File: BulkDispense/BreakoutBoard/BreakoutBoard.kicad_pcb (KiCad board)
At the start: 2 copper layers, 170 x 100.5 mm, 33 parts, among them J1 Bubble Sensor Power, J10 Reagent Media Valve Signal, J11 Proportional Control Valve, J12 Reagent Media Valve GND, J13 Pressure Sensor, J14 Waste 2/2 Media Valve GND, J15 Waste 2/2 Media Valve Power, J16 Waste 3/2 Media Valve, J17 Waste Bottle Sensor 1, J18 Waste Line Sensor 2, J19 Waste Line Sensor 1, J2 Bubble Sensor Signal, J20 Waste Bottle Sensor 2, J21 Waste Vacuum Sensor 1, J22 Waste Vacuum Sensor 2, J23 MAXI Power, J24 Waste 2/2 Media Valve Power, J25 Waste 2/2 Media Valve GND, J26 Waste Line Sensor 1, J27 Waste Line Sensor 2, J28 Waste Bottle Sensor 1, J29 Waste Bottle Sensor 2, J3 Bubble Sensor GND, J30 Waste 3/2 Media Valve, J31 Waste Vacuum Sensor 1, J32 Waste Vacuum Sensor 2, J33 37212-62M3-003PL, J4 Overflow Sensor Power, J5 Overflow Sensor GND, J6 Overflow Sensor Signal, J7 Input Power, J8 Reagent Valve Power, J9 Reagent Valve GND

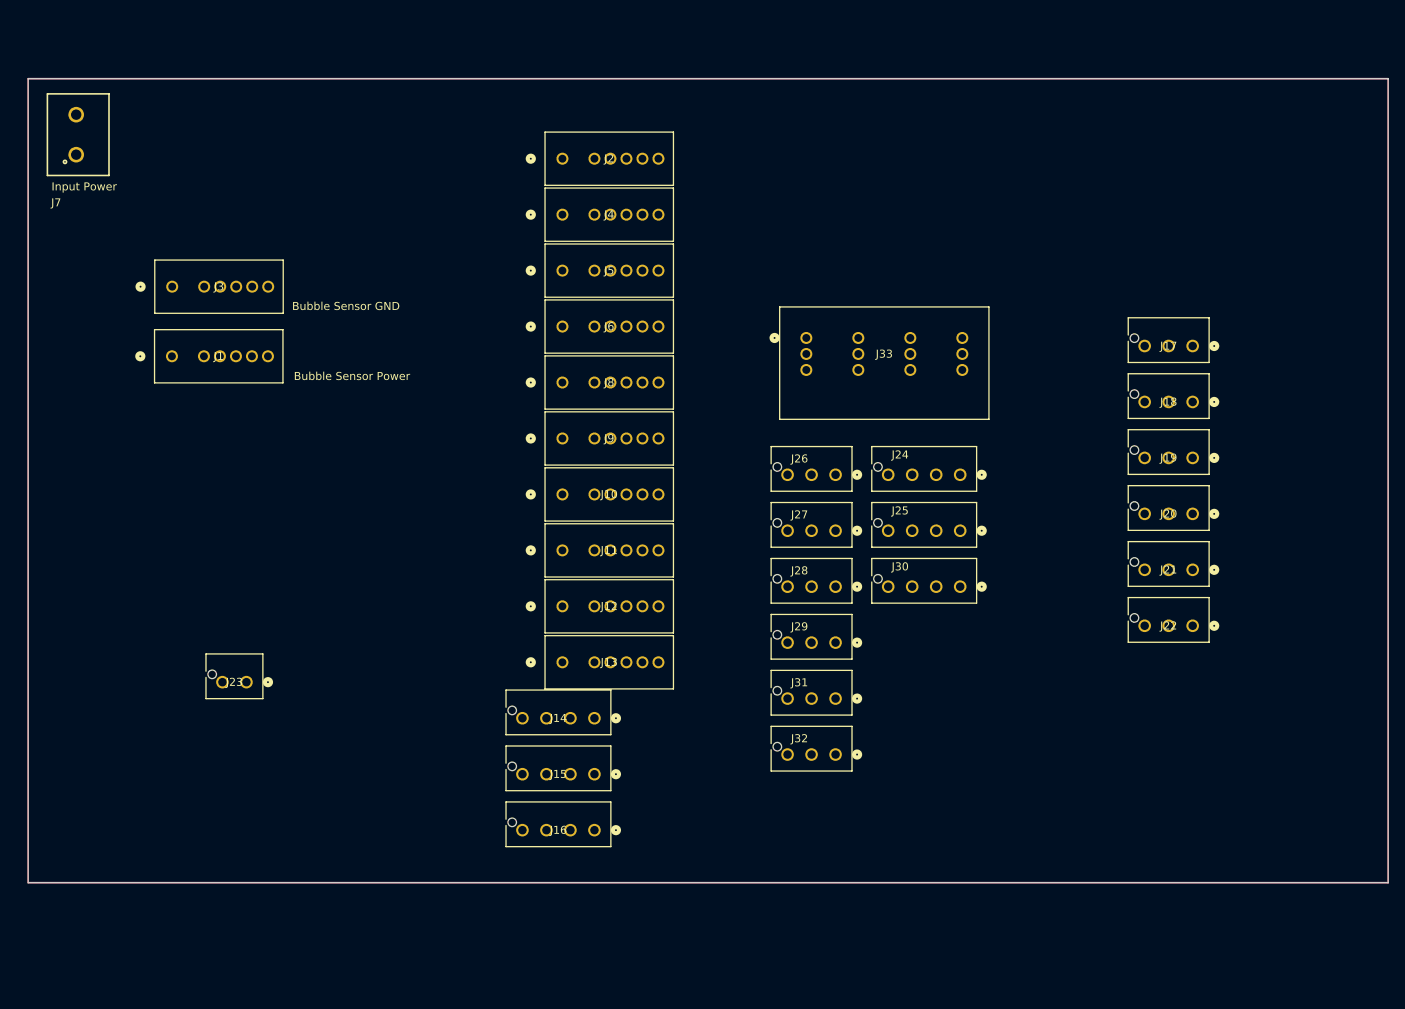
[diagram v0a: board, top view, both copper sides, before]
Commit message: Update 3POS Connectors with Mini-Clamp
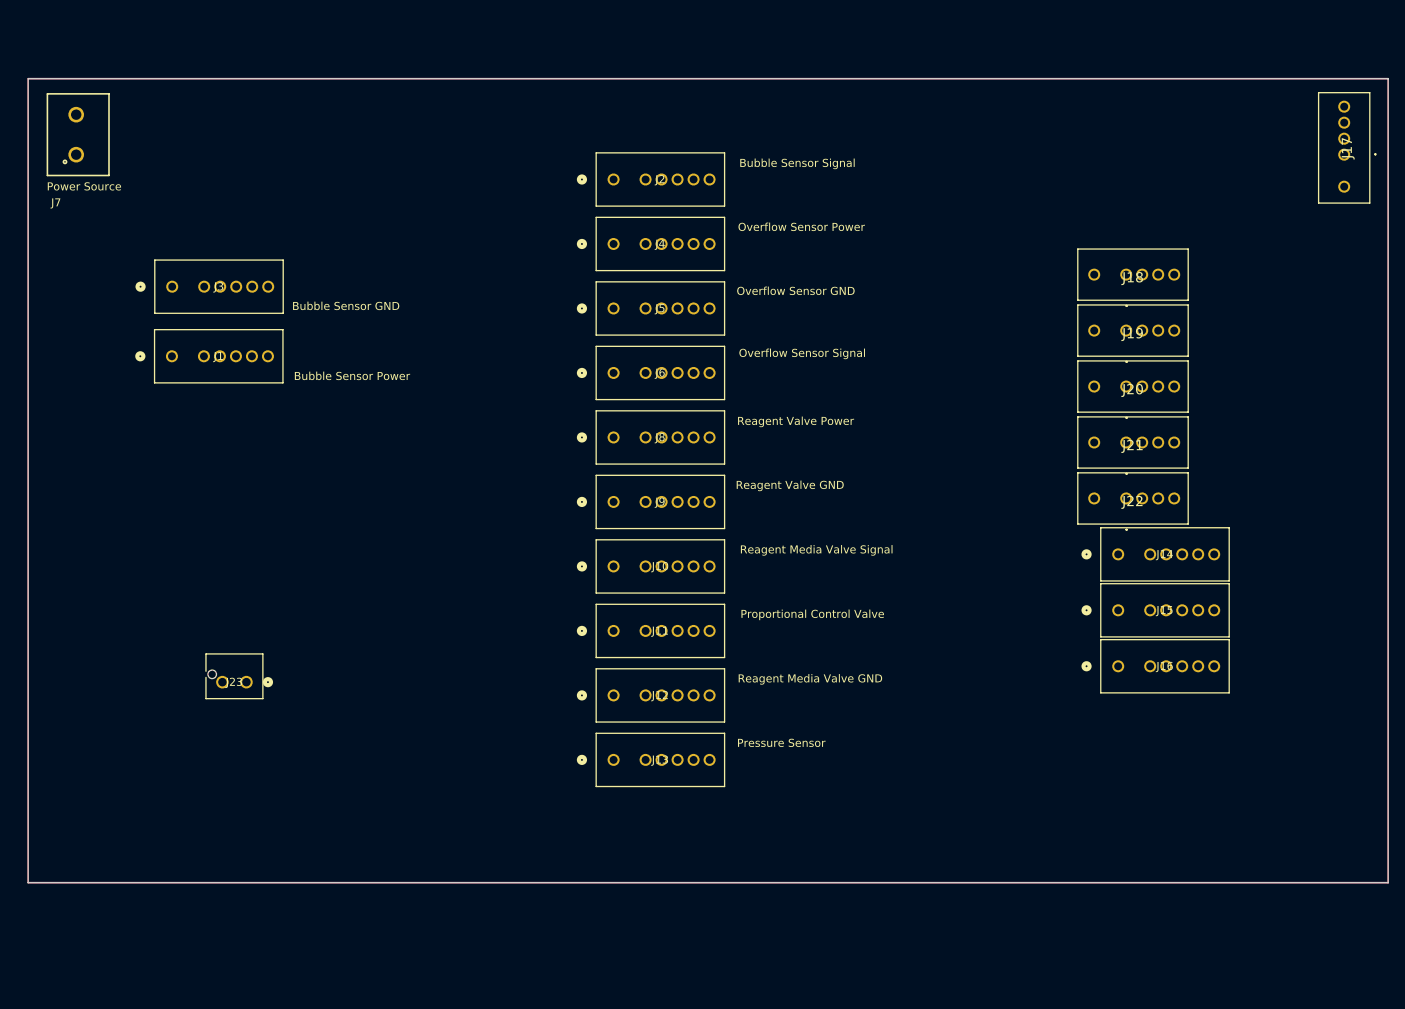
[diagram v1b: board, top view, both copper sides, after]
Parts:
- removed J24: Waste 2/2 Media Valve Power, PartsLibrary:CONN04_2165712004_MOL
- removed J25: Waste 2/2 Media Valve GND, PartsLibrary:CONN04_2165712004_MOL
- removed J26: Waste Line Sensor 1, PartsLibrary:CONN03_2165711003_MOL
- removed J27: Waste Line Sensor 2, PartsLibrary:CONN03_2165711003_MOL
- removed J28: Waste Bottle Sensor 1, PartsLibrary:CONN03_2165711003_MOL
- removed J29: Waste Bottle Sensor 2, PartsLibrary:CONN03_2165711003_MOL
- removed J30: Waste 3/2 Media Valve, PartsLibrary:CONN04_2165712004_MOL
- removed J31: Waste Vacuum Sensor 1, PartsLibrary:CONN03_2165711003_MOL
- removed J32: Waste Vacuum Sensor 2, PartsLibrary:CONN03_2165711003_MOL
- removed J33: 37212-62M3-003PL, PartsLibrary:CONN_37212-62M3-003PL_3MM
- J14, J15, J16: footprint PartsLibrary:CONN04_2165712004_MOL -> PartsLibrary:CONN_37204-62A3-004PL_3MM
- J17, J18, J19, J20, J21, J22: footprint PartsLibrary:CONN03_2165711003_MOL -> PartsLibrary:3720362A3003PL
- J7: value Input Power -> Power Source
- moved J14 72.4 mm to (191.7, 96.5)
- moved J15 72.4 mm to (191.7, 103.5)
- moved J16 72.4 mm to (191.7, 110.4)
- moved J17 30.5 mm to (216.0, 46.5), turned to 90 degrees
- moved J18 18.0 mm to (188.8, 61.5)
- moved J19 18.0 mm to (188.8, 68.5)
- moved J20 18.0 mm to (188.8, 75.5)
- moved J21 18.0 mm to (188.8, 82.5)
- moved J22 18.0 mm to (188.8, 89.5)
- moved J13 13.8 mm to (128.7, 122.2)
- moved J12 12.8 mm to (128.7, 114.1)
- moved J11 11.9 mm to (128.7, 106.0)
- moved J10 11.0 mm to (128.7, 98.0)
- moved J9 10.2 mm to (128.7, 89.9)
- moved J8 9.38 mm to (128.7, 81.8)
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
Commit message: First Draft of BreakoutBoard
- Included MAXI Expansion Board Starter
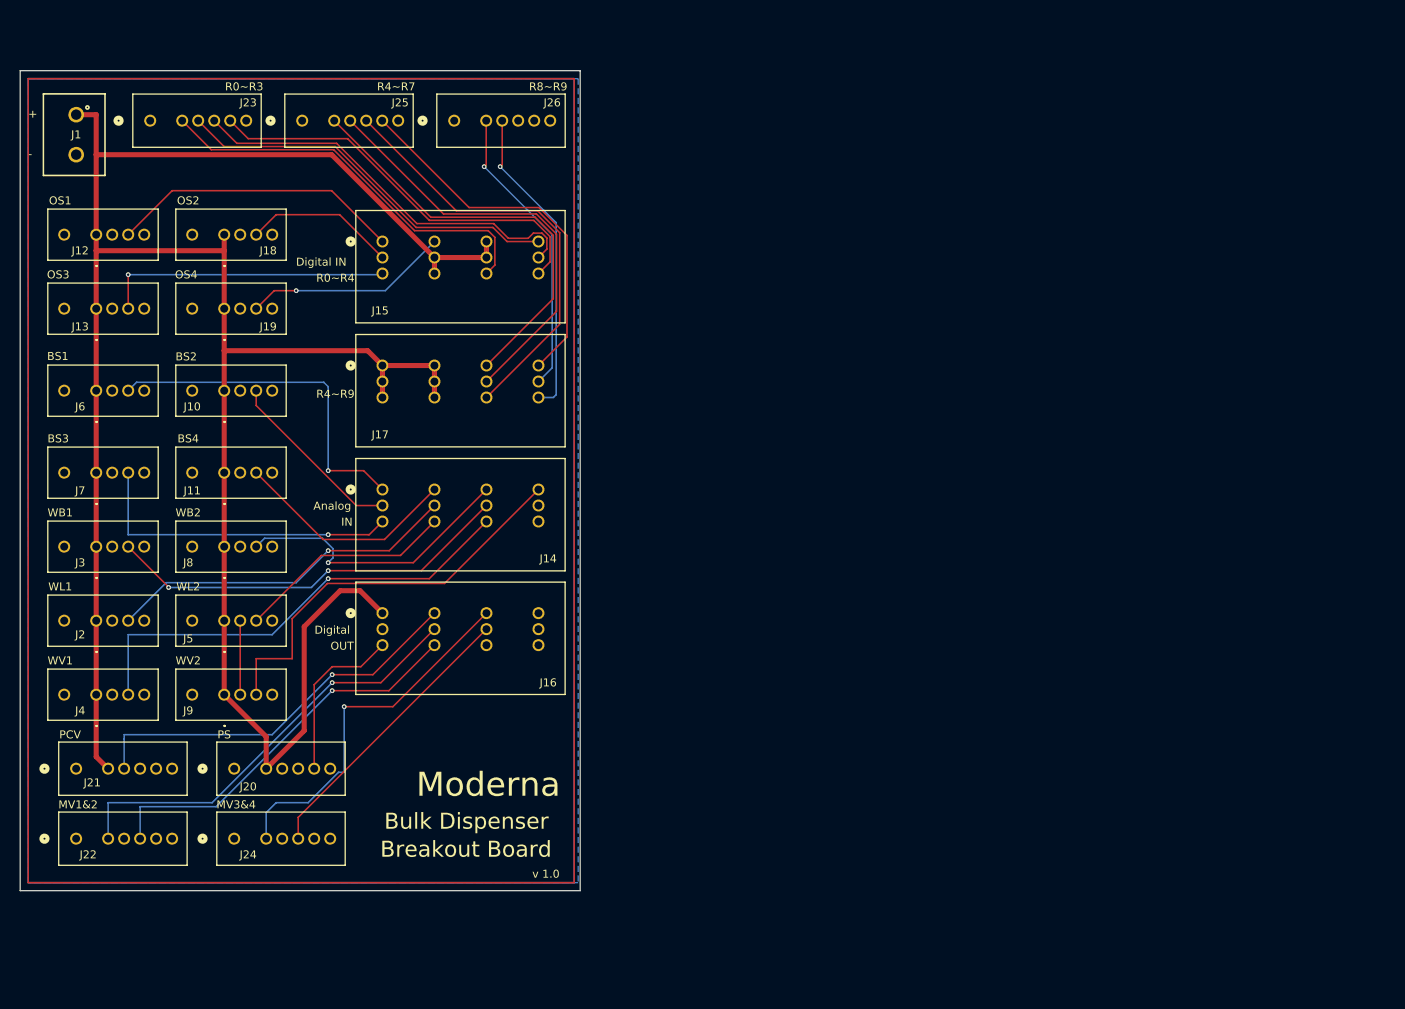
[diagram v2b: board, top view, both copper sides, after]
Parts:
- removed the J1 at (73.5, 71.7)
- added J24: MV3&4, PartsLibrary:CONN_37204-62A3-004PL_3MM, F.Cu at (81.2, 132.0)
- added J25: R4~R7, PartsLibrary:CONN_37204-62A3-004PL_3MM, F.Cu at (89.8, 42.2)
- added J26: R8~R9, PartsLibrary:CONN_37204-62A3-004PL_3MM, F.Cu at (108.8, 42.2)
- added J7: BS3, PartsLibrary:3720362A3003PL, F.Cu at (60.0, 86.2)
- J10: value Reagent Media Valve Signal -> BS2; footprint PartsLibrary:CONN_37204-62A3-004PL_3MM -> PartsLibrary:3720362A3003PL
- J11: value Proportional Control Valve -> BS4; footprint PartsLibrary:CONN_37204-62A3-004PL_3MM -> PartsLibrary:3720362A3003PL
- J12: value Reagent Media Valve GND -> OS1; footprint PartsLibrary:CONN_37204-62A3-004PL_3MM -> PartsLibrary:3720362A3003PL
- J13: value Pressure Sensor -> OS3; footprint PartsLibrary:CONN_37204-62A3-004PL_3MM -> PartsLibrary:3720362A3003PL
- J14: value Waste 2/2 Media Valve GND -> Analog Inputs; footprint PartsLibrary:CONN_37204-62A3-004PL_3MM -> PartsLibrary:CONN_37212-62M3-003PL_3MM
- J15: value Waste 2/2 Media Valve Power -> Digital IN + R0~R4; footprint PartsLibrary:CONN_37204-62A3-004PL_3MM -> PartsLibrary:CONN_37212-62M3-003PL_3MM
- J16: value Waste 3/2 Media Valve -> Digital Outputs; footprint PartsLibrary:CONN_37204-62A3-004PL_3MM -> PartsLibrary:CONN_37212-62M3-003PL_3MM
- J17: value Waste Bottle Sensor 1 -> R4~R9; footprint PartsLibrary:3720362A3003PL -> PartsLibrary:CONN_37212-62M3-003PL_3MM
- J18: value Waste Line Sensor 2 -> OS2
- J19: value Waste Line Sensor 1 -> OS4
- J2: value Bubble Sensor Signal -> WL1; footprint PartsLibrary:CONN_37204-62A3-004PL_3MM -> PartsLibrary:3720362A3003PL
- J20: value Waste Bottle Sensor 2 -> PS; footprint PartsLibrary:3720362A3003PL -> PartsLibrary:CONN_37204-62A3-004PL_3MM
- J21: value Waste Vacuum Sensor 1 -> PCV; footprint PartsLibrary:3720362A3003PL -> PartsLibrary:CONN_37204-62A3-004PL_3MM
- J22: value Waste Vacuum Sensor 2 -> MV1&2; footprint PartsLibrary:3720362A3003PL -> PartsLibrary:CONN_37204-62A3-004PL_3MM
- J23: value MAXI Power -> R0~R3; footprint PartsLibrary:CONN02_2165711002_MOL -> PartsLibrary:CONN_37204-62A3-004PL_3MM
- J3: value Bubble Sensor GND -> WB1; footprint PartsLibrary:CONN_37204-62A3-004PL_3MM -> PartsLibrary:3720362A3003PL
- J4: value Overflow Sensor Power -> WV1; footprint PartsLibrary:CONN_37204-62A3-004PL_3MM -> PartsLibrary:3720362A3003PL
- J5: value Overflow Sensor GND -> WL2; footprint PartsLibrary:CONN_37204-62A3-004PL_3MM -> PartsLibrary:3720362A3003PL
- J6: value Overflow Sensor Signal -> BS1; footprint PartsLibrary:CONN_37204-62A3-004PL_3MM -> PartsLibrary:3720362A3003PL
- J8: value Reagent Valve Power -> WB2; footprint PartsLibrary:CONN_37204-62A3-004PL_3MM -> PartsLibrary:3720362A3003PL
- J9: value Reagent Valve GND -> WV2; footprint PartsLibrary:CONN_37204-62A3-004PL_3MM -> PartsLibrary:3720362A3003PL
- moved J22 134.2 mm to (61.5, 132.0)
- moved J21 133.6 mm to (61.5, 123.2)
- moved J17 123.1 mm to (95.8, 72.9), turned to 0 degrees
- moved J20 117.6 mm to (81.2, 123.2)
- moved J18 112.9 mm to (76.0, 56.5)
- moved J19 112.8 mm to (76.0, 65.8)
- moved J15 106.5 mm to (95.8, 57.4)
- moved J14 96.3 mm to (95.8, 88.4)
- moved J16 96.2 mm to (95.8, 103.8)
- moved J12 89.6 mm to (60.0, 56.5)
- moved J13 88.9 mm to (60.0, 65.8)
- moved J4 88.8 mm to (60.0, 114.0)
- moved J2 88.1 mm to (60.0, 104.8)
- moved J23 70.6 mm to (70.8, 42.2)
- moved J6 68.7 mm to (60.0, 76.0)
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- renumbered J7 to J1
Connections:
- J10 pad 1: /DO3 -> +24V
- J10 pad 2: /DO2 -> GND
- J10 pad 3: /DO1 -> /AI1
- J11 pad 2: /AI13 -> GND
- J11 pad 3: /AO0 -> /AI3
- J12 pad 1: GND -> +24V
- J12 pad 3: GND -> /DI0
- J13 pad 3: GND -> /DI2
- J14 pad 1: GND -> /AI0
- J14 pad 2: GND -> /AI1
- J14 pad 3: GND -> /AI2
- J14 pad 4: GND -> /AI3
- J14 pad 5: (no net) -> /AI4
- J14 pad 6: (no net) -> /AI5
- J15 pad 1: +24V -> /DI0
- J15 pad 2: +24V -> /DI1
- J15 pad 3: +24V -> /DI2
- J15 pad 4: +24V -> /DI3
- J15 pad 5: (no net) -> +24V
- J15 pad 6: (no net) -> +24V
- J16 pad 2: +24V -> GND
- J16 pad 3: GND -> /AI12
- J16 pad 4: GND -> /AI13
- J16 pad 5: (no net) -> /DO0
- J16 pad 6: (no net) -> /DO1
- J17 pad 2: GND -> +24V
- J17 pad 3: /AI7 -> +24V
- J18 pad 3: /AI5 -> /DI1
- J19 pad 3: /AI4 -> /DI3
- J2 pad 1: /AI3 -> +24V
- J2 pad 2: /AI2 -> GND
- J2 pad 3: /AI1 -> /AI4
- J20 pad 3: /AI6 -> GND
- J21 pad 2: GND -> /AI13
- J21 pad 3: /AI8 -> /AO0
- J22 pad 1: +24V -> /DO0
- J22 pad 3: /AI9 -> /DO1
- J23 pad 1: +24V -> /R0_OUT
- J23 pad 2: GND -> /R1_OUT
- J3 pad 1: GND -> +24V
- J3 pad 3: GND -> /AI7
- J4 pad 2: +24V -> GND
- J4 pad 3: +24V -> /AI8
- J5 pad 1: GND -> +24V
- J5 pad 3: GND -> /AI5
- J6 pad 1: /DI3 -> +24V
- J6 pad 2: /DI2 -> GND
- J6 pad 3: /DI1 -> /AI0
- J8 pad 2: +24V -> GND
- J8 pad 3: +24V -> /AI6
- J9 pad 1: GND -> +24V
- J9 pad 3: GND -> /AI9
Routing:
- net +24V: track 0.00 -> 295.5 mm
- net /AI8: track 0.00 -> 58.3 mm, vias 0 -> 1
- net /R6_OUT: track 0.00 -> 54.4 mm
- net /DO0: track 0.00 -> 54.3 mm, vias 0 -> 1
- net /R5_OUT: track 0.00 -> 53.7 mm
- net /R4_OUT: track 0.00 -> 53.1 mm
- net /AI9: track 0.00 -> 51.5 mm
- net /R3_OUT: track 0.00 -> 51.2 mm
- net /AI7: track 0.00 -> 51.2 mm, vias 0 -> 2
- net /R2_OUT: track 0.00 -> 51.1 mm
- net /R0_OUT: track 0.00 -> 50.1 mm
- net /AI13: track 0.00 -> 49.3 mm, vias 0 -> 1
- net /DO1: track 0.00 -> 49.2 mm, vias 0 -> 1
- net /R1_OUT: track 0.00 -> 48.8 mm
- net /R7_OUT: track 0.00 -> 46.8 mm
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- added copper zone on B.Cu, net GND
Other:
- board size 170 x 100.5 mm -> 70 x 102.5 mm
- board text added: "+"
- board text added: "-"
- board text added: "Analog"
- board text added: "Breakout Board"
- board text added: "Bulk Dispenser"
- board text added: "Digital"
- board text added: "Digital IN"
- board text added: "IN"
- board text added: "Moderna"
- board text added: "OUT"
- board text added: "R0~R4"
- board text added: "R4~R9"
- board text added: "v 1.0"

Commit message: Add more documentation + holding mounts
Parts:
- added H1: MountingHole, MountingHole:MountingHole_2.2mm_M2, F.Cu at (120.5, 37.0)
- added H2: MountingHole, MountingHole:MountingHole_2.2mm_M2, F.Cu at (51.5, 37.0)
- added H3: MountingHole, MountingHole:MountingHole_2.2mm_M2, F.Cu at (121.0, 137.0)
- added H4: MountingHole, MountingHole:MountingHole_2.2mm_M2, F.Cu at (51.5, 137.0)
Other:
- board size 70 x 102.5 mm -> 72.5 x 103 mm

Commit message: Finished Up Board + MAXIExpansionBoard
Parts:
- removed the J1 at (57.5, 44.0)
- added D1: LED, LED_SMD:LED_1206_3216Metric, F.Cu at (172.9, 38.2)
- added J12: FS1, PartsLibrary:CONN_37204-62A3-004PL_3MM, F.Cu at (118.2, 117.2)
- added J13: FS3, PartsLibrary:CONN_37204-62A3-004PL_3MM, F.Cu at (118.2, 126.2)
- added J15: FS2, PartsLibrary:CONN_37204-62A3-004PL_3MM, F.Cu at (136.9, 117.2)
- added J16: FS4, PartsLibrary:CONN_37204-62A3-004PL_3MM, F.Cu at (136.9, 126.2)
- added J30: Flow Sensors, PartsLibrary:CONN_37212-62M3-003PL_3MM, F.Cu at (153.2, 129.1)
- added R1: R, Resistor_SMD:R_0805_2012Metric, F.Cu at (173.4, 40.8)
- moved H4 129.0 mm to (179.9, 149.8)
- moved H2 128.4 mm to (179.9, 34.0)
- moved J3 58.5 mm to (117.9, 48.2)
- moved J4 58.5 mm to (133.9, 48.2)
- moved J8 58.5 mm to (117.9, 78.2)
- moved J9 58.5 mm to (133.9, 78.2)
- moved J1 58.4 mm to (117.9, 68.2)
- moved J2 58.4 mm to (133.9, 68.2)
- moved J10 58.4 mm to (117.9, 58.2)
- moved J11 58.4 mm to (133.9, 58.2)
- moved J24 58.4 mm to (117.9, 88.2)
- moved J25 58.4 mm to (133.9, 88.2)
- moved J17 58.3 mm to (117.9, 98.2)
- moved J18 58.3 mm to (133.9, 98.2)
- moved J28 58.2 mm to (117.9, 108.2)
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- renumbered J6 to J1, J13 to J10, J19 to J11, J21 to J14, J2 to J17, J5 to J18, J14 to J19, J10 to J2, J23 to J20, J25 to J21, J26 to J22, J15 to J23, J3 to J24, J8 to J25, J16 to J26, J17 to J27, J4 to J28, J9 to J29, J12 to J3, J18 to J4, J20 to J5, J22 to J6, J24 to J7, J7 to J8, J11 to J9
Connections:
- J17 pad 3: /AI4 -> /AI6
- J18 pad 3: /AI5 -> /AI7
- J19 pad 11: /AI10 -> /FS1-1
- J19 pad 12: /AI11 -> /FS1-2
- J24 pad 3: /AI7 -> /AI4
- J25 pad 3: /AI6 -> /AI5
- J26 pad 10: /DO5 -> /FS1-4
- J26 pad 11: /DO6 -> /FS2-1
- J26 pad 12: /DO7 -> /FS2-2
- J26 pad 9: /DO4 -> /FS1-3
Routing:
- net /DO1: track 49.2 -> 121.7 mm, vias 1 -> 0
- net /DO0: track 54.3 -> 126.8 mm, vias 1 -> 0
- net /FS1-1: track 0.00 -> 64.4 mm, vias 0 -> 1
- net /FS1-2: track 0.00 -> 62.3 mm, vias 0 -> 1
- net /AO0: track 0.00 -> 58.7 mm
- net /DO3: track 35.9 -> 91.4 mm
- net /FS1-4: track 0.00 -> 54.2 mm, vias 0 -> 1
- net /FS3-2: track 0.00 -> 51.4 mm
- net /DO2: track 45.9 -> 96.6 mm, vias 1 -> 0
- net /FS3-3: track 0.00 -> 49.5 mm
- net /FS3-4: track 0.00 -> 48.2 mm
- net /FS1-3: track 0.00 -> 45.8 mm, vias 0 -> 1
- net /FS3-1: track 0.00 -> 40.2 mm
- net /FS4-4: track 0.00 -> 39.8 mm, vias 0 -> 1
- net /FS2-2: track 0.00 -> 38.9 mm
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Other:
- board size 72.5 x 103 mm -> 74.5 x 119 mm
- board text added: "Analog IN"
- board text added: "Controllino"
- board text added: "Digital OUT"
- board text added: "Outbound"
- board text added: "Plumbing"
- board text added: "Power"
- board text removed: "+"
- board text removed: "-"
- board text removed: "Analog"
- board text removed: "Digital"
- board text removed: "IN"
- board text removed: "OUT"

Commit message: Add STEP files
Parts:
- J30: value Flow Sensors -> Flow Sensors (PORT2)
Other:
- board text added: "Analog IN (PORT4)"
- board text added: "Digital OUT (PORT1)"
- board text added: "R0~R4 (PORT3)"
- board text added: "R4~R9 (PORT5)"
- board text removed: "Analog IN"
- board text removed: "Digital OUT"
- board text removed: "R0~R4"
- board text removed: "R4~R9"
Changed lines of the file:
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@@
 			)
 		)
-		(property "Value" "Flow Sensors"
-			(at 1.716598 -5.103901 0)
+		(property "Value" "Flow Sensors (PORT2)\n"
+			(at 4.806348 -5.103901 0)
 			(unlocked yes)
 			(layer "F.SilkS")
@@
 		(layer "Edge.Cuts")
 	)
-	(gr_text "Digital OUT"
+	(gr_text "Digital OUT (PORT1)"
 		(at 149.41025 106 0)
 		(layer "F.SilkS")
@@
 		)
 	)
-	(gr_text "R0~R4"
+	(gr_text "R0~R4 (PORT3)"
 		(at 149.41025 50.25 0)
 		(layer "F.SilkS")
@@
 		)
 	)
-	(gr_text "Analog IN"
+	(gr_text "Analog IN (PORT4)"
 		(at 149.66025 87.25 0)
 		(layer "F.SilkS")
@@
 		)
 	)
-	(gr_text "R4~R9"
+	(gr_text "R4~R9 (PORT5)"
 		(at 149.41025 68.75 0)
 		(layer "F.SilkS")
